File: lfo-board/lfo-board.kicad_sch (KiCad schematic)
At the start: 0 parts

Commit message: wip
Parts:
- added J1, J2: Conn_01x20, Connector_PinSocket_2.54mm:PinSocket_1x20_P2.54mm_Vertical, symbol Connector_Generic:Conn_01x20
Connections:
- new net +4.5V: J1.12 (Pin_12), J1.16 (Pin_16), J1.3 (Pin_3), J1.8 (Pin_8), J2.12 (Pin_12), J2.16 (Pin_16), J2.3 (Pin_3), J2.8 (Pin_8)
- new net +9V: J1.1 (Pin_1), J2.1 (Pin_1)
- new net Freq1: J1.6 (Pin_6), J2.6 (Pin_6)
- new net Freq2: J1.7 (Pin_7), J2.7 (Pin_7)
- new net GND: J1.13 (Pin_13), J1.18 (Pin_18), J1.2 (Pin_2), J1.5 (Pin_5), J1.9 (Pin_9), J2.13 (Pin_13), J2.18 (Pin_18), J2.2 (Pin_2), J2.5 (Pin_5), J2.9 (Pin_9)
- new net Offset1: J1.10 (Pin_10), J2.10 (Pin_10)
- new net Offset2: J1.11 (Pin_11), J2.11 (Pin_11)
- new net Out: J1.4 (Pin_4), J2.4 (Pin_4)
- new net Sync: J1.19 (Pin_19), J2.19 (Pin_19)
- new net Tap: J1.20 (Pin_20), J2.20 (Pin_20)
- new net WForm1: J1.14 (Pin_14), J2.14 (Pin_14)
- new net WForm2: J1.15 (Pin_15), J2.15 (Pin_15)
- new net WFormOf: J1.17 (Pin_17), J2.17 (Pin_17)
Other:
- sheet LFO ports: added +4.5V, +5V, +9V, DepthCV, FreqCV, GND, OffsetCV, Out, TapIn, WaveformCV; removed none
- sheet io ports: added +4.5V, +5V, +9V, Depth1, Depth2, DepthOut, DepthVof, Freq1, Freq2, FreqOut, FreqVof, GND, Offset1, Offset2, OffsetOut, OffsetVof, Sync, TapOut, WForm1, WForm2, WFormOut, WFormVof; removed none

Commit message: Before removing attenuverters
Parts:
- J1, J2: value Conn_01x20 -> Conn_01x25; footprint Connector_PinSocket_2.54mm:PinSocket_1x20_P2.54mm_Vertical -> Connector_PinSocket_2.54mm:PinSocket_1x25_P2.54mm_Vertical; symbol Connector_Generic:Conn_01x20 -> Connector_Generic:Conn_01x25
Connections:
- net +4.5V: now also J1.13 (Pin_13); no longer J1.12 (Pin_12), J1.16 (Pin_16), J2.12 (Pin_12), J2.16 (Pin_16), J2.8 (Pin_8)
- net Freq1: no longer J2.6 (Pin_6)
- net Freq2: no longer J2.7 (Pin_7)
- net FreqOf: now also J1.9 (Pin_9)
- net GND: now also J1.10 (Pin_10), J1.15 (Pin_15); no longer J1.13 (Pin_13), J1.18 (Pin_18), J1.9 (Pin_9), J2.13 (Pin_13), J2.18 (Pin_18), J2.9 (Pin_9)
- net Offset1: now also J1.11 (Pin_11); no longer J1.10 (Pin_10), J2.10 (Pin_10)
- net Offset2: now also J1.12 (Pin_12); no longer J1.11 (Pin_11), J2.11 (Pin_11)
- net OffsetOf: now also J1.14 (Pin_14)
- net Sync: no longer J1.19 (Pin_19), J2.19 (Pin_19)
- net Tap: no longer J1.20 (Pin_20), J2.20 (Pin_20)
- net WForm1: no longer J1.14 (Pin_14), J2.14 (Pin_14)
- net WForm2: no longer J1.15 (Pin_15), J2.15 (Pin_15)
- net WFormOf: no longer J1.17 (Pin_17), J2.17 (Pin_17)

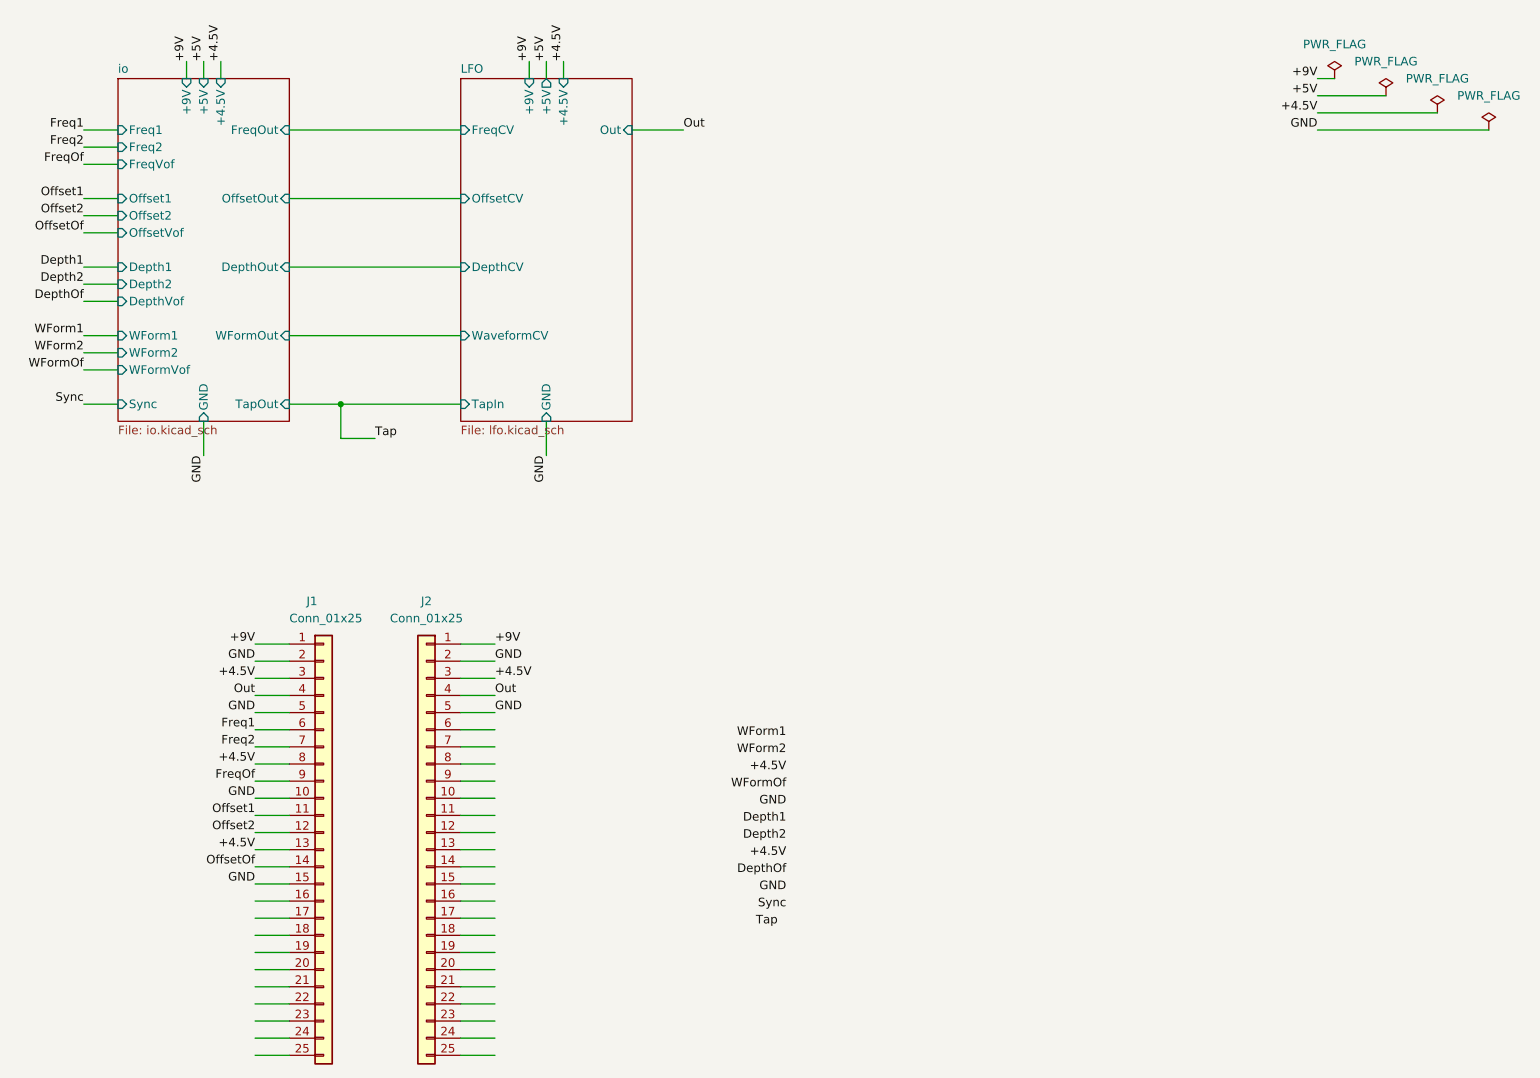
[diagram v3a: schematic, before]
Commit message: LFO graphics
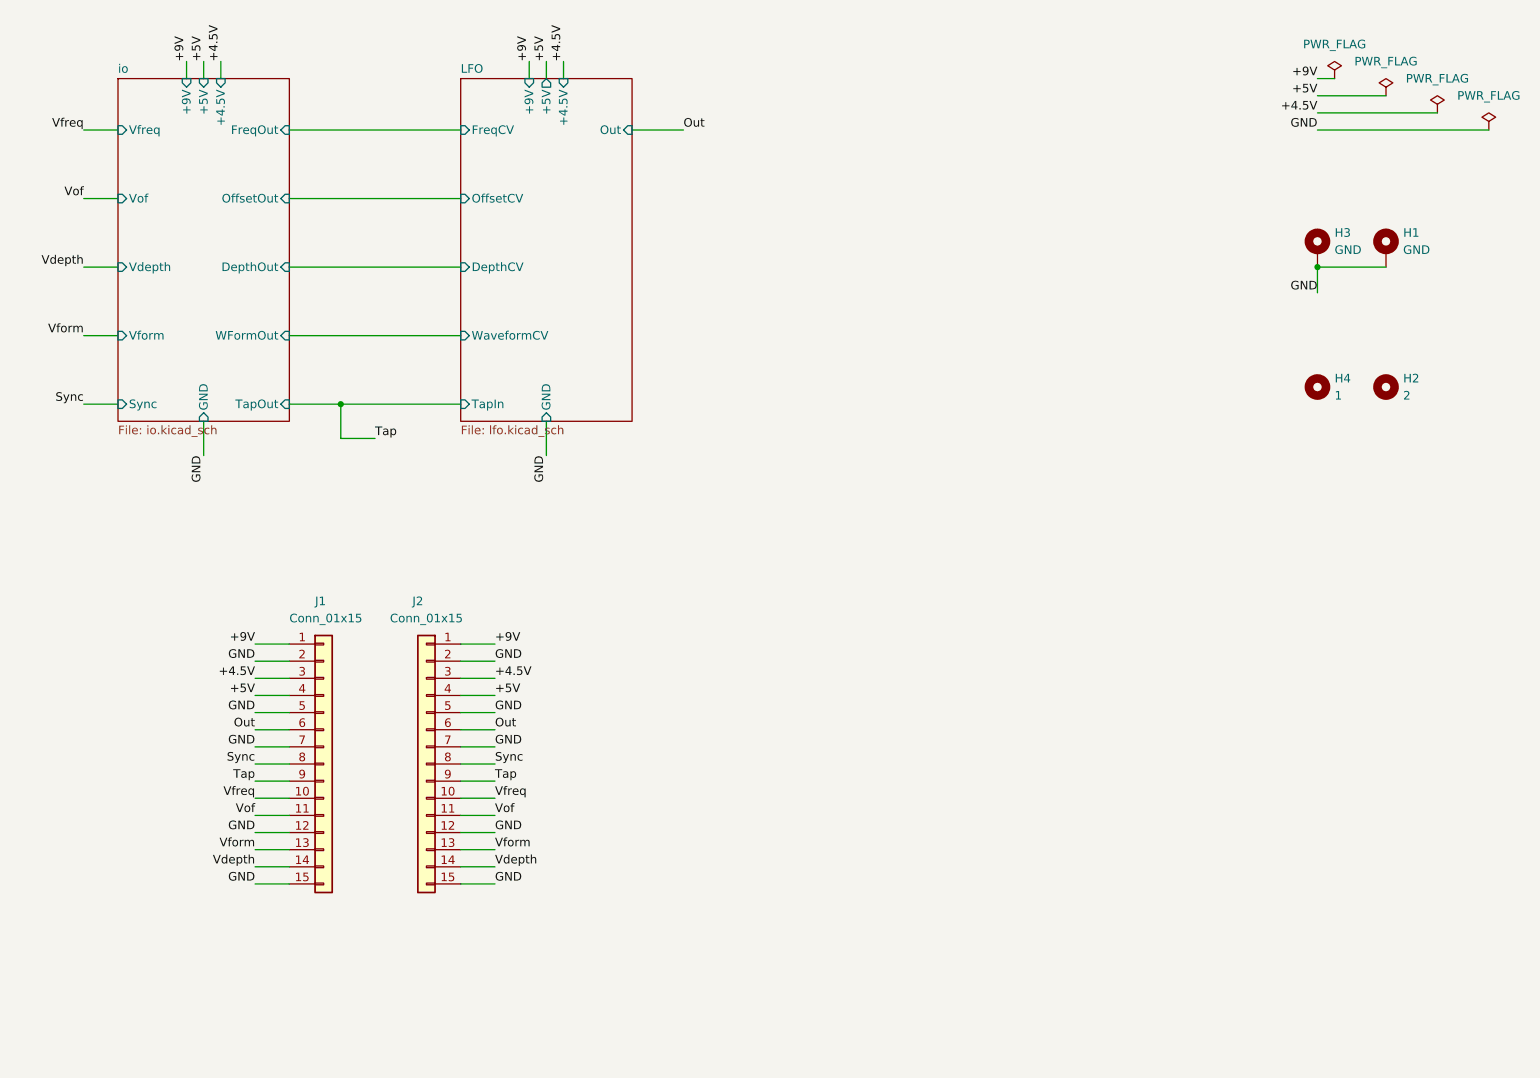
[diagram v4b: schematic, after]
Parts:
- added H1, H3: GND, MountingHole:MountingHole_3.2mm_M3_ISO14580_Pad, symbol Mechanical:MountingHole_Pad
- added H2: 2, MountingHole:MountingHole_3.2mm_M3, symbol Mechanical:MountingHole
- added H4: 1, MountingHole:MountingHole_3.2mm_M3, symbol Mechanical:MountingHole
- J1, J2: value Conn_01x25 -> Conn_01x15; footprint Connector_PinSocket_2.54mm:PinSocket_1x25_P2.54mm_Vertical -> Connector_PinSocket_2.54mm:PinSocket_1x15_P2.54mm_Vertical; symbol Connector_Generic:Conn_01x25 -> Connector_Generic:Conn_01x15
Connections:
- net Freq1 is gone; now on net Out: J1.6 (Pin_6)
- net Freq2 is gone; now on net GND: J1.7 (Pin_7)
- net FreqOf is gone; now on net Tap: J1.9 (Pin_9)
- net Offset1 is gone; now on net Vof: J1.11 (Pin_11)
- net Offset2 is gone; now on net GND: J1.12 (Pin_12)
- net OffsetOf is gone; now on net Vdepth: J1.14 (Pin_14)
- net +4.5V: no longer J1.13 (Pin_13), J1.8 (Pin_8)
- net +5V: now also J1.4 (Pin_4), J2.4 (Pin_4)
- net GND: now also J2.12 (Pin_12), J2.15 (Pin_15), J2.7 (Pin_7), H1.1, H3.1; no longer J1.10 (Pin_10)
- net Out: now also J2.6 (Pin_6); no longer J1.4 (Pin_4), J2.4 (Pin_4)
- net Sync: now also J1.8 (Pin_8), J2.8 (Pin_8)
- net Tap: now also J2.9 (Pin_9)
- net Vfreq: now reaches J2.10 (Pin_10)
- net Vfreq: now also J1.10 (Pin_10)
- net Vof: now reaches J2.11 (Pin_11)
- net Vform: now reaches J2.13 (Pin_13)
- net Vform: now also J1.13 (Pin_13)
- net Vdepth: now reaches J2.14 (Pin_14)
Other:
- sheet io ports: added Vdepth, Vform, Vfreq, Vof; removed Depth1, Depth2, DepthVof, Freq1, Freq2, FreqVof, Offset1, Offset2, OffsetVof, WForm1, WForm2, WFormVof

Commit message: wip pre-redo orientation
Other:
- company: (none) -> Andrey Salomatin / Pedal Markt
- title: (none) -> Longwave
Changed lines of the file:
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@@
 (kicad_sch (version 20211123) (generator eeschema)
   (paper "A4")
+  (title_block
+    (title "Longwave")
+    (date "2024-12-18")
+    (rev "v1rev2")
+    (company "Andrey Salomatin / Pedal Markt")
+  )
   (junction (at 83.82 73.66) (diameter 0) (color 0 0 0 0)
   )
